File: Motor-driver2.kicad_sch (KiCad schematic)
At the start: 56 parts, among them J10 PINHD_1x3_Male, J11 PINHD_1x3_Male, J12 PINHD_1x4_Male, J13 PINHD_1x3_Male, J14 PINHD_1x3_Male, J15 PINHD_1x4_Male, U4 DRV8825PWP, U5 DRV8825PWP

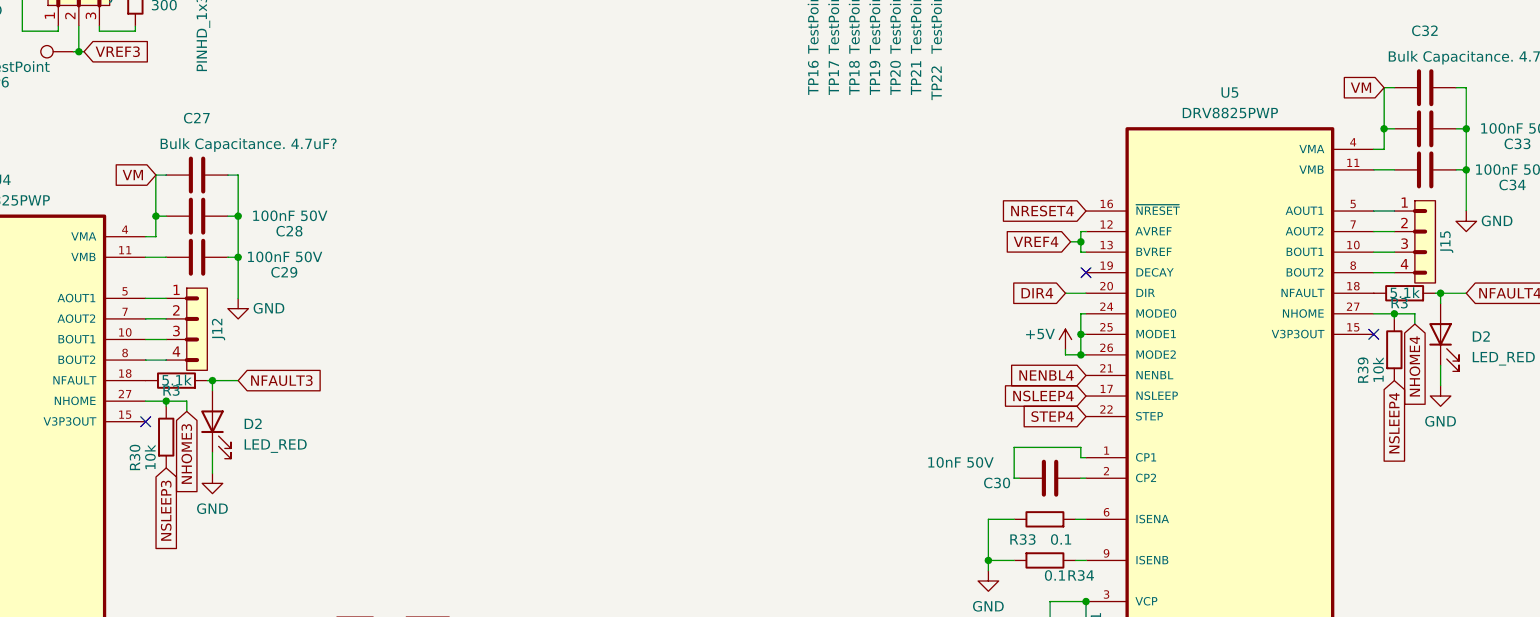
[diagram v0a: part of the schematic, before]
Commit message: fixed few errors, added test points
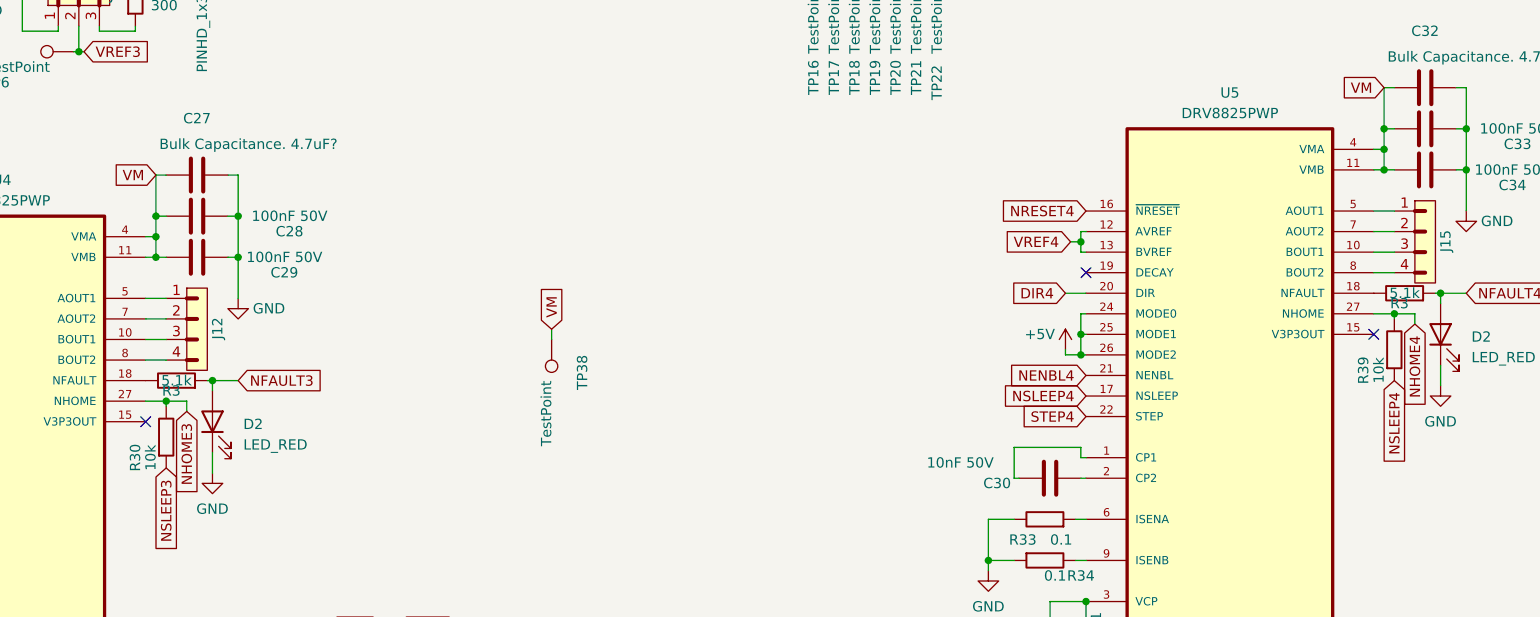
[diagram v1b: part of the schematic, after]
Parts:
- added TP38: TestPoint, TestPoint:TestPoint_Pad_D2.5mm, symbol Connector:TestPoint
- C26: footprint TestPoint:TestPoint_Pad_D2.5mm -> Capacitor_SMD:C_01005_0402Metric
- C31: footprint (none) -> Capacitor_SMD:C_01005_0402Metric
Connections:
- net VM: now also C29.1, C34.1, U4.11 (VMB), U5.11 (VMB), TP38.1
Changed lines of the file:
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@@
   (junction (at 240.665 77.47) (diameter 0) (color 0 0 0 0)
   )
+  (junction (at 240.665 80.01) (diameter 0) (color 0 0 0 0)
+  )
   (junction (at 95.885 108.585) (diameter 0) (color 0 0 0 0)
   )
   (junction (at 51.435 113.665) (diameter 0) (color 0 0 0 0)
   )
+  (junction (at 88.9 90.805) (diameter 0) (color 0 0 0 0)
+  )
   (junction (at 247.65 97.79) (diameter 0) (color 0 0 0 0)
   )
@@
   (junction (at 203.835 135.89) (diameter 0) (color 0 0 0 0)
   )
+  (junction (at 240.665 82.55) (diameter 0) (color 0 0 0 0)
+  )
   (junction (at 88.9 88.265) (diameter 0) (color 0 0 0 0)
+  )
+  (junction (at 88.9 93.345) (diameter 0) (color 0 0 0 0)
   )
   (junction (at 250.825 77.47) (diameter 0) (color 0 0 0 0)
@@
     (stroke (width 0) (type default))
   )
+  (wire (pts (xy 88.9 90.805) (xy 87.63 90.805))
+    (stroke (width 0) (type default))
+  )
   (wire (pts (xy 230.505 34.29) (xy 230.505 34.925))
     (stroke (width 0) (type default))
@@
     (stroke (width 0) (type default))
   )
-  (wire (pts (xy 88.9 90.805) (xy 87.63 90.805))
+  (wire (pts (xy 87.63 93.345) (xy 88.9 93.345))
     (stroke (width 0) (type default))
   )
@@
     (stroke (width 0) (type default))
   )
+  (wire (pts (xy 240.665 82.55) (xy 241.935 82.55))
+    (stroke (width 0) (type default))
+  )
   (wire (pts (xy 180.975 31.75) (xy 182.88 31.75))
     (stroke (width 0) (type default))
@@
     (stroke (width 0) (type default))
   )
+  (wire (pts (xy 88.9 93.345) (xy 90.17 93.345))
+    (stroke (width 0) (type default))
+  )
   (wire (pts (xy 72.39 47.625) (xy 76.835 47.625))
     (stroke (width 0) (type default))
@@
     (stroke (width 0) (type default))
   )
+  (wire (pts (xy 137.795 103.505) (xy 137.795 102.235))
+    (stroke (width 0) (type default))
+  )
   (wire (pts (xy 51.435 102.235) (xy 50.165 102.235))
     (stroke (width 0) (type default))
@@
     (stroke (width 0) (type default))
   )
-  (wire (pts (xy 239.395 82.55) (xy 241.935 82.55))
+  (wire (pts (xy 239.395 82.55) (xy 240.665 82.55))
     (stroke (width 0) (type default))
   )
@@
     (stroke (width 0) (type default))
   )
+  (wire (pts (xy 240.665 80.01) (xy 240.665 82.55))
+    (stroke (width 0) (type default))
+  )
   (wire (pts (xy 67.945 56.515) (xy 68.58 56.515))
     (stroke (width 0) (type default))
@@
     (stroke (width 0) (type default))
   )
+  (wire (pts (xy 88.9 90.805) (xy 88.9 93.345))
+    (stroke (width 0) (type default))
+  )
   (wire (pts (xy 116.84 146.685) (xy 118.745 146.685))
     (stroke (width 0) (type default))
@@
     (stroke (width 0) (type default))
   )
-  (wire (pts (xy 87.63 93.345) (xy 90.17 93.345))
-    (stroke (width 0) (type default))
-  )
   (wire (pts (xy 201.295 105.41) (xy 201.295 104.775))
     (stroke (width 0) (type default))
@@
     )
   )
+  (global_label "VM" (shape input) (at 137.795 102.235 90) (fields_autoplaced)
+    (effects (font (size 1.27 1.27)) (justify left))
+    (property "Intersheetrefs" "${INTERSHEET_REFS}" (at 137.795 96.7098 90)
+      (effects (font (size 1.27 1.27)) (justify left) hide)
+    )
+  )
   (global_label "PB13" (shape input) (at 180.975 26.67 180) (fields_autoplaced)
     (effects (font (size 1.27 1.27)) (justify right))
@@
     (property "Intersheetrefs" "${INTERSHEET_REFS}" (at 41.7672 118.745 0)
       (effects (font (size 1.27 1.27)) (justify right) hide)
+    )
+  )
+  (symbol (lib_id "Connector:TestPoint") (at 137.795 103.505 180) (unit 1)
+    (in_bom yes) (on_board yes) (dnp no)
+    (property "Reference" "TP38" (at 141.605 105.41 90)
+      (effects (font (size 1.27 1.27)) (justify left))
+    )
+    (property "Value" "TestPoint" (at 137.16 108.585 90)
+      (effects (font (size 1.27 1.27)) (justify left))
+    )
+    (property "Footprint" "TestPoint:TestPoint_Pad_D2.5mm" (at 132.715 103.505 0)
+      (effects (font (size 1.27 1.27)) hide)
+    )
+    (property "Datasheet" "~" (at 132.715 103.505 0)
+      (effects (font (size 1.27 1.27)) hide)
+    )
+    (pin "1")
+    (instances
+      (project "Doodle Drive"
+        (path "/3ec634aa-8c09-482d-9325-2288a4dbd68b"
+          (reference "TP38") (unit 1)
+        )
+        (path "/3ec634aa-8c09-482d-9325-2288a4dbd68b/4a4951fa-be57-4d48-97a5-6be750b353b5"
+          (reference "TP40") (unit 1)
+        )
+      )
     )
   )
@@
       (effects (font (size 1.27 1.27)) (justify left))
     )
-    (property "Footprint" "TestPoint:TestPoint_Pad_D2.5mm" (at 51.1048 149.225 0)
+    (property "Footprint" "Capacitor_SMD:C_01005_0402Metric" (at 51.1048 149.225 0)
       (effects (font (size 1.27 1.27)) hide)
     )
@@
       (effects (font (size 1.27 1.27)) (justify left))
     )
-    (property "Footprint" "" (at 202.8698 138.43 0)
-      (effects (font (size 1.27 1.27)) hide)
-    )
+    (property "Footprint" "Capacitor_SMD:C_01005_0402Metric" (at 202.8698 138.43 0)
+      (effects (font (size 1.27 1.27)) hide)
+    )

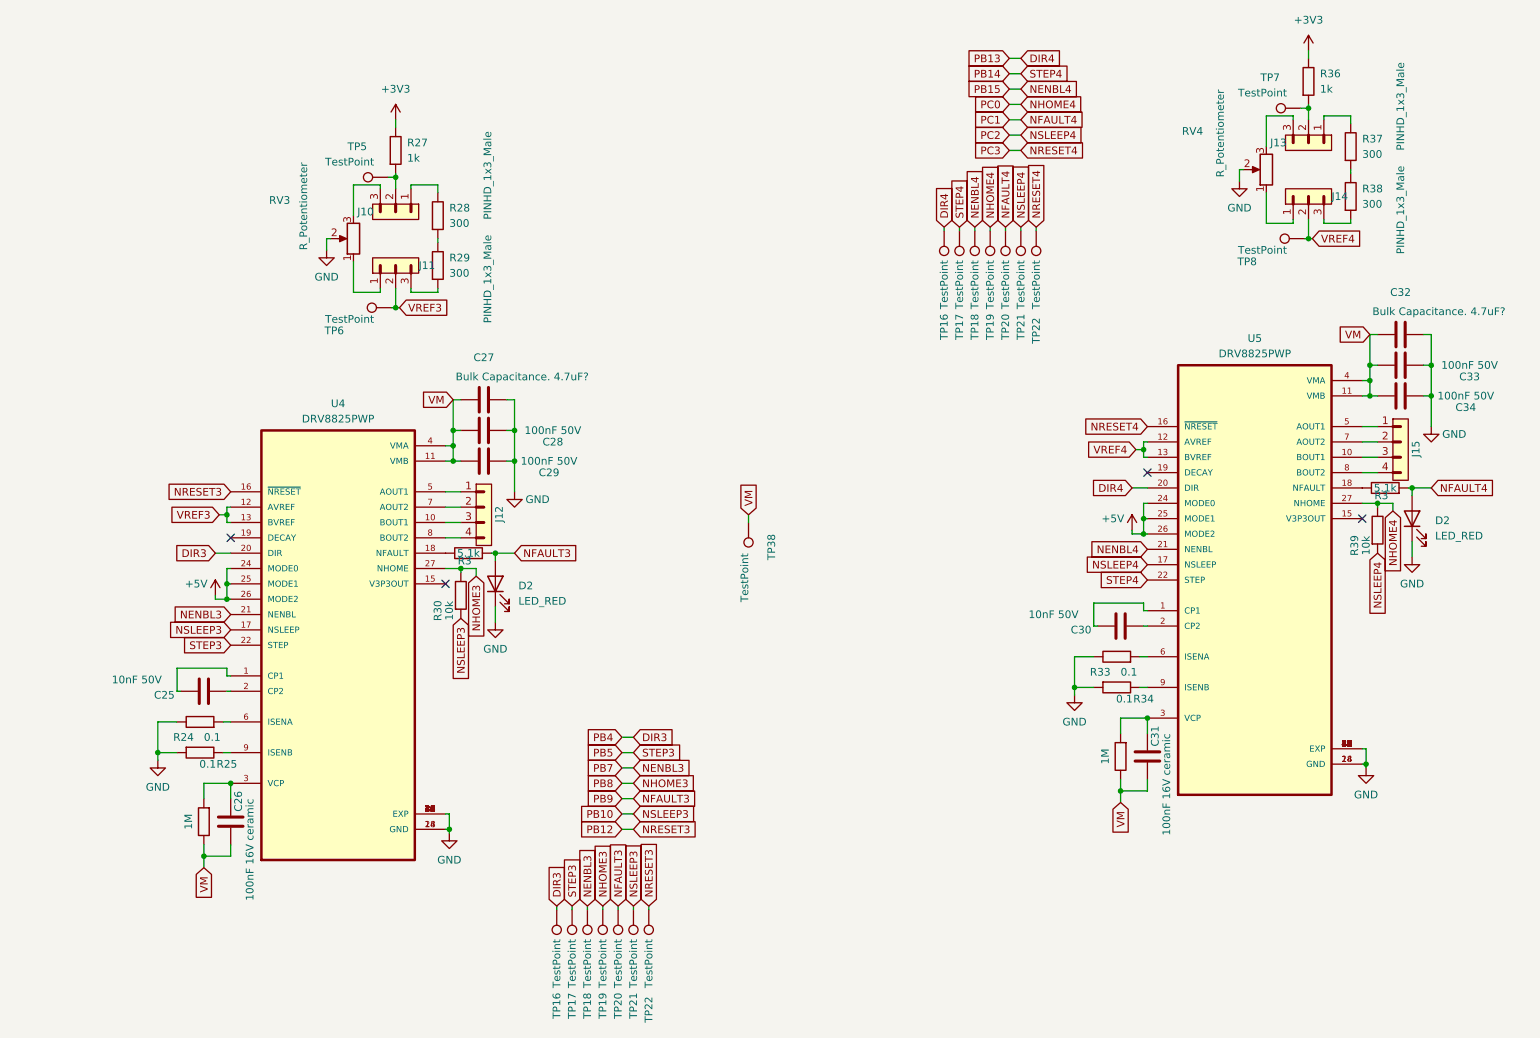
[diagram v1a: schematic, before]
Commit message: add CP2102 USB to UART chip
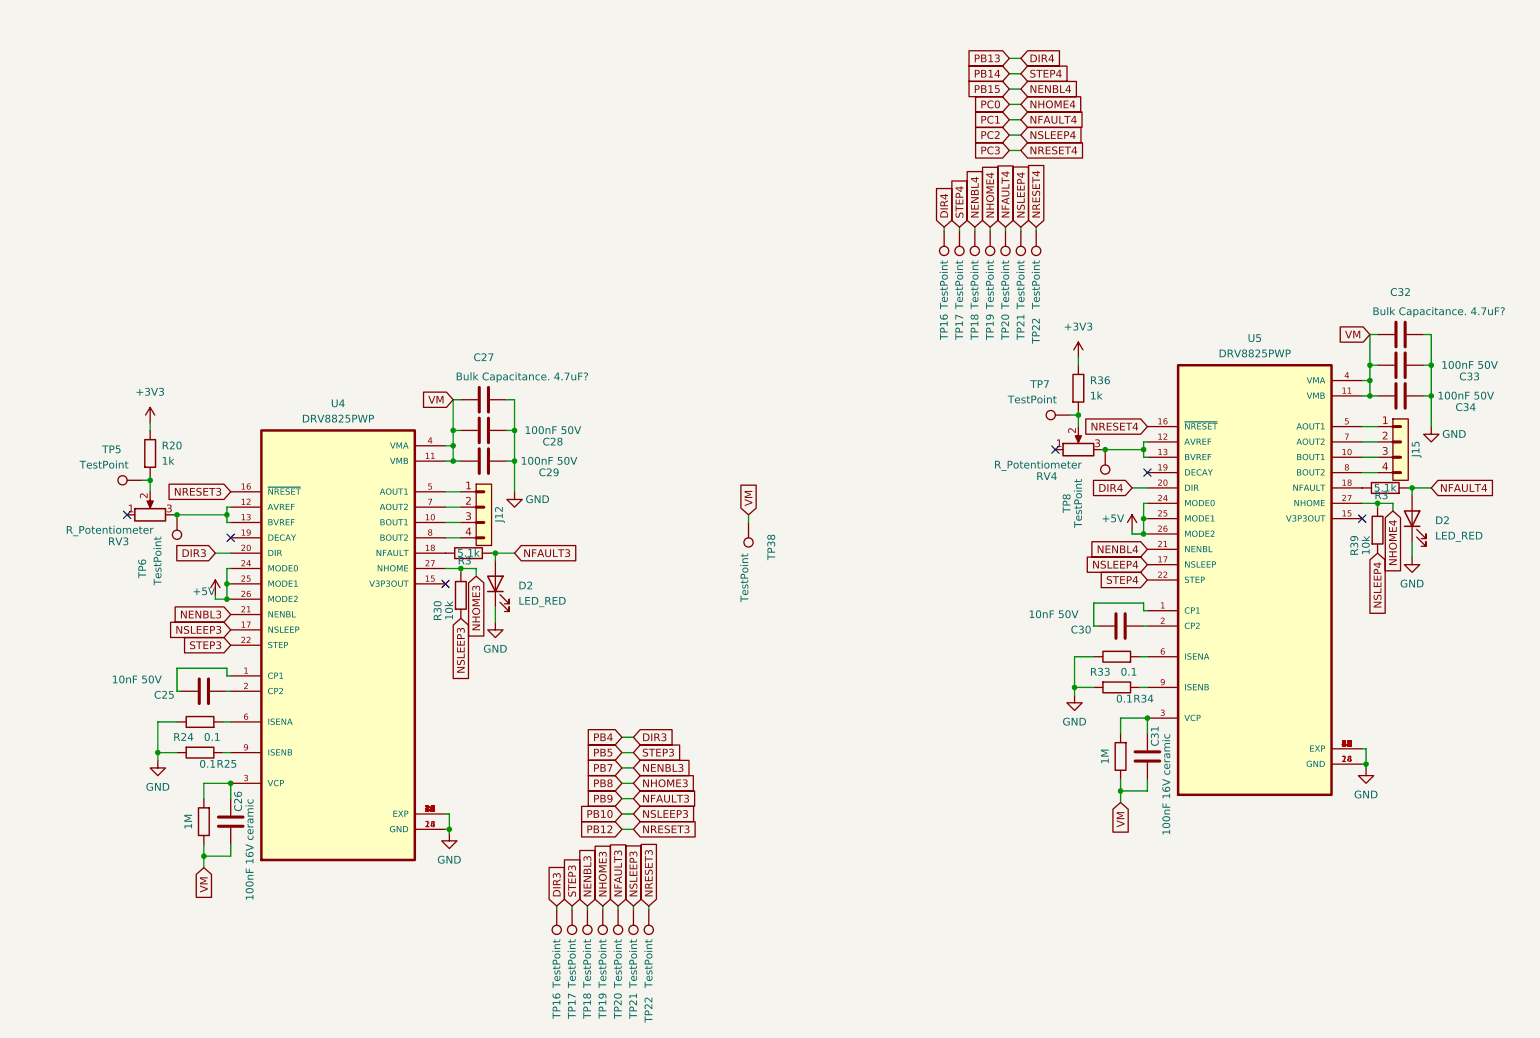
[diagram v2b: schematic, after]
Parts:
- removed J10, J11, J13, J14: PINHD_1x3_Male, Connector_PinHeader_2.54mm:PinHeader_1x03_P2.54mm_Vertical, symbol PCM_SL_Pin_Headers:PINHD_1x3_Male
- removed R27: 1k, Resistor_SMD:R_0805_2012Metric, symbol PCM_SL_Devices:Resistor
- removed R28, R29, R37, R38: 300, Resistor_SMD:R_0805_2012Metric, symbol PCM_SL_Devices:Resistor
- added R20: 1k, Resistor_SMD:R_0805_2012Metric, symbol PCM_SL_Devices:Resistor
- RV3, RV4: footprint (none) -> Potentiometer_THT:Potentiometer_ACP_CA6-H2,5_Horizontal
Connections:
- net VREF3 is gone; now on an unnamed net: TP6.1, U4.12 (AVREF), U4.13 (BVREF)
- net VREF4 is gone; now on an unnamed net: TP8.1, U5.12 (AVREF), U5.13 (BVREF)
- net +3V3: now also R20.2
- net GND: no longer RV3.2, RV4.2
- net at R36.1, TP7.1: now also RV4.2
- net at TP5.1: now also RV3.2, R20.1
- no-connect marks 4 -> 6
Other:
- moved on the sheet: R36, RV4, TP7, TP8
